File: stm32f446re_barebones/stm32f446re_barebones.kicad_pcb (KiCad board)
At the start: 2 copper layers, 38 parts, among them J1 Lin pots connector, J2 gyro/accel connectors( maybe ), J3 USB_B_Mini, J4 Uart pins, J5 SWD, J6 SPI connectors, SW1 SW_SPDT, SW2 SW_Push, U1 STM32F446RETx, U2 AMS1117-3.3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

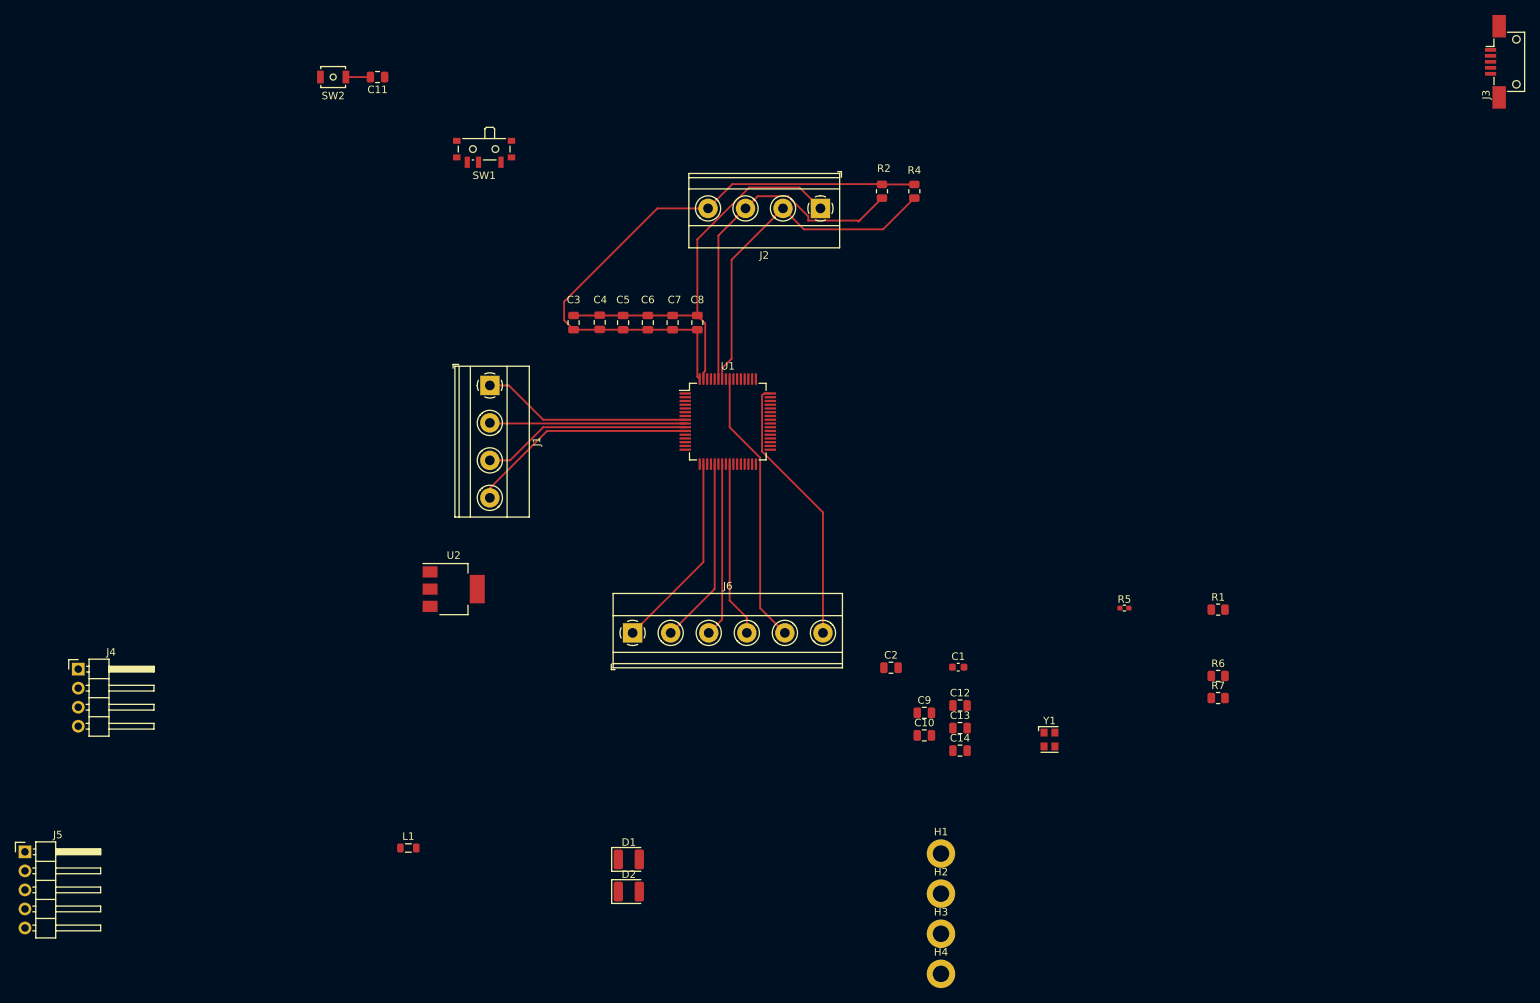
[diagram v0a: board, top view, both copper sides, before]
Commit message: PCB routing. Need to do USB differential pair. Also usb maybe backwards
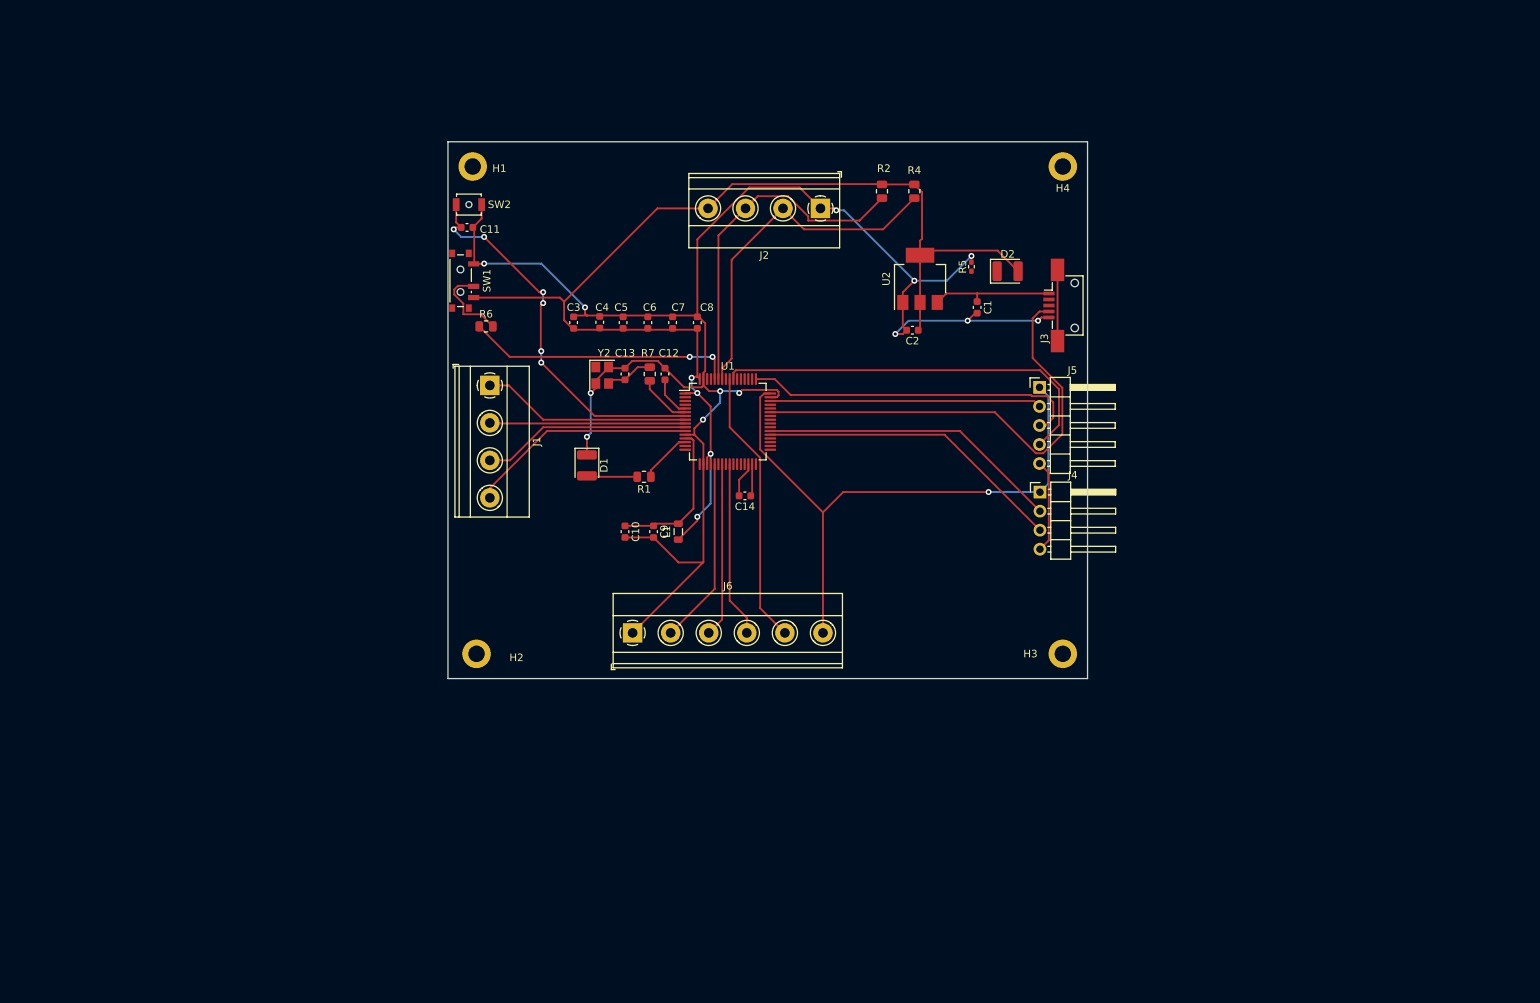
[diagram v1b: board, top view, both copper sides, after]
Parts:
- removed Y1: 16mhz, Oscillator:Oscillator_SMD_Kyocera_KC2520Z-4Pin_2.5x2.0mm
- added Y2: Y2, Crystal:Crystal_SMD_3225-4Pin_3.2x2.5mm, F.Cu at (120.7, 71.3)
- C10, C11, C12, C13, C14, C2, C3, C4, C5, C6, C7, C8, C9: footprint Capacitor_SMD:C_0805_2012Metric -> Capacitor_SMD:C_0603_1608Metric
- moved J5 148.9 mm to (179.0, 72.9)
- moved J4 130.5 mm to (179.1, 86.9)
- moved H1 110.9 mm to (103.4, 43.4)
- moved H4 108.9 mm to (182.1, 43.4), turned to 180 degrees
- moved R6 108.2 mm to (105.2, 64.8)
- moved D2 97.0 mm to (174.8, 57.4)
- moved R7 87.3 mm to (127.0, 71.1), turned to -90 degrees
- moved R1 78.6 mm to (126.2, 84.8), turned to 180 degrees
- moved U2 74.7 mm to (163.1, 58.4), turned to 90 degrees
- moved H2 69.8 mm to (103.9, 108.5), turned to 180 degrees
- moved J3 67.3 mm to (181.9, 62.0)
- moved C13 65.0 mm to (123.7, 71.1), turned to 90 degrees
- moved C12 59.2 mm to (129.0, 71.1), turned to 90 degrees
- moved L1 55.5 mm to (130.8, 92.2), turned to 90 degrees
- moved D1 52.9 mm to (118.6, 83.3), turned to -90 degrees
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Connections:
- J4 pad 2: USART6_TX -> USART6_RX
- J4 pad 3: USART6_RX -> USART6_TX
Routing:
- net GND: track 85.8 -> 250.5 mm, vias 0 -> 13
- net +3.3V: track 117.0 -> 238.0 mm, vias 0 -> 5
- net USB_ID: track 0.00 -> 61.9 mm
- net SWO: track 0.00 -> 53.9 mm
- net NRST: track 0.00 -> 51.6 mm, vias 0 -> 6
- net SWCLK: track 0.00 -> 45.3 mm
- net USART6_TX: track 0.00 -> 41.3 mm
- net USART6_RX: track 0.00 -> 40.4 mm
- net SWDIO: track 0.00 -> 36.2 mm
- net BOOT0: track 0.00 -> 35.9 mm, vias 0 -> 2
- net +3.3VA: track 0.00 -> 20.4 mm
- net VBUS: track 0.00 -> 16.5 mm
- net Net-(SW1-B): track 0.00 -> 11.2 mm
- net unconnected-(J3-Shield-Pad6): track 0.00 -> 9.50 mm
- net HSE_OUT: track 0.00 -> 8.04 mm
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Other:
- board outline added: 85.3 x 71.6 mm

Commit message: tweaked some stuff for the daq and added a files
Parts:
- J3: footprint Connector_USB:USB_Mini-B_AdamTech_MUSB-B5-S-VT-TSMT-1_SMD_Vertical -> Connector_USB:USB_Mini-B_Lumberg_2486_01_Horizontal
- turned J3 to 90 degrees
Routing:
- net GND: track 250.5 -> 273.0 mm
- net HSE_IN: track 5.48 -> 26.1 mm, vias 0 -> 2
- net unconnected-(J3-Shield-Pad6): track 9.50 -> 21.1 mm
- net VBUS: track 16.5 -> 23.5 mm
- net USB_ID: track 61.9 -> 66.0 mm, vias 0 -> 2
- net USB-: track 0.00 -> 1.24 mm
